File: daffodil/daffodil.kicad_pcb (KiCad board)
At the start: 2 copper layers, 70.7 x 53.3 mm, 8 parts, among them J1 NEIGHBOR1, J2 NEIGHBOR2, J7 BONUS_ROW, P1 GREATFET-PROTO-AREA

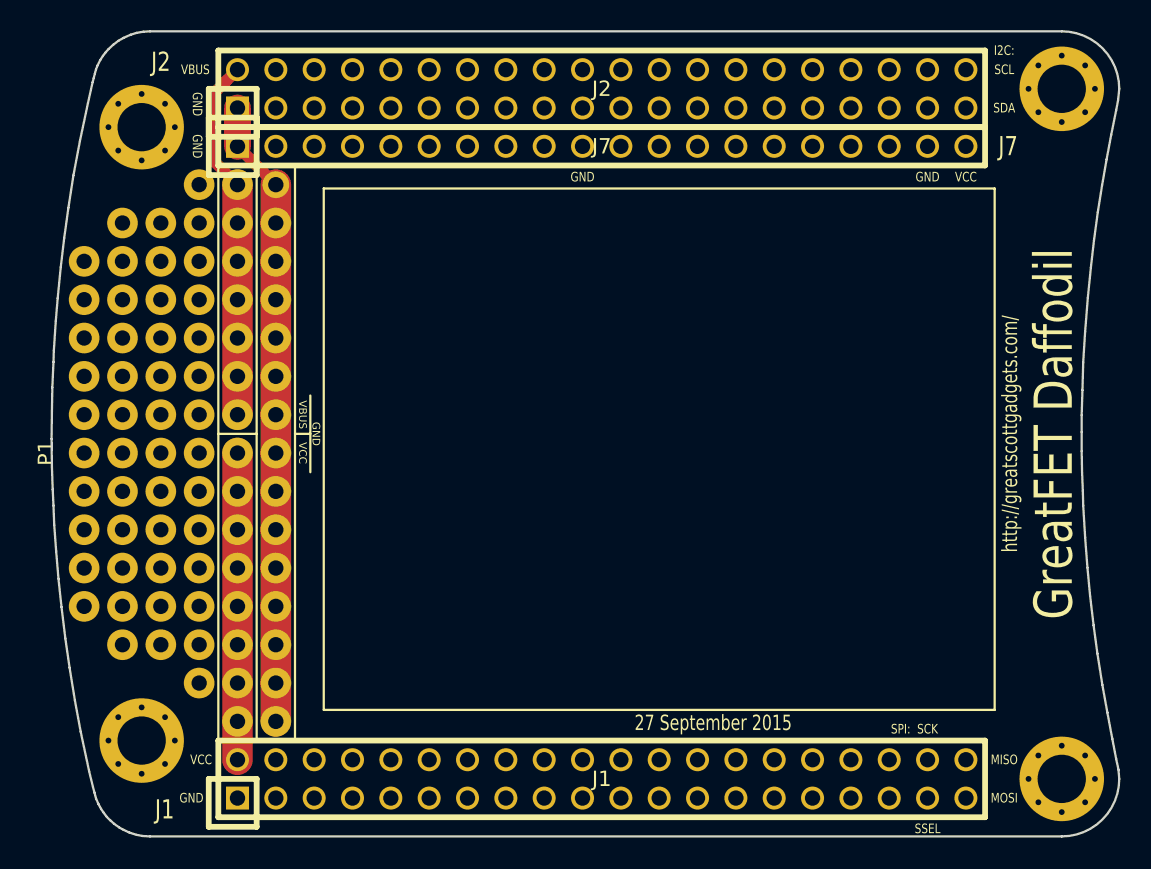
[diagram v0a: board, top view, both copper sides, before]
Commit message: Daffodil: removed GND from J7 pin 10, updated silkscreen
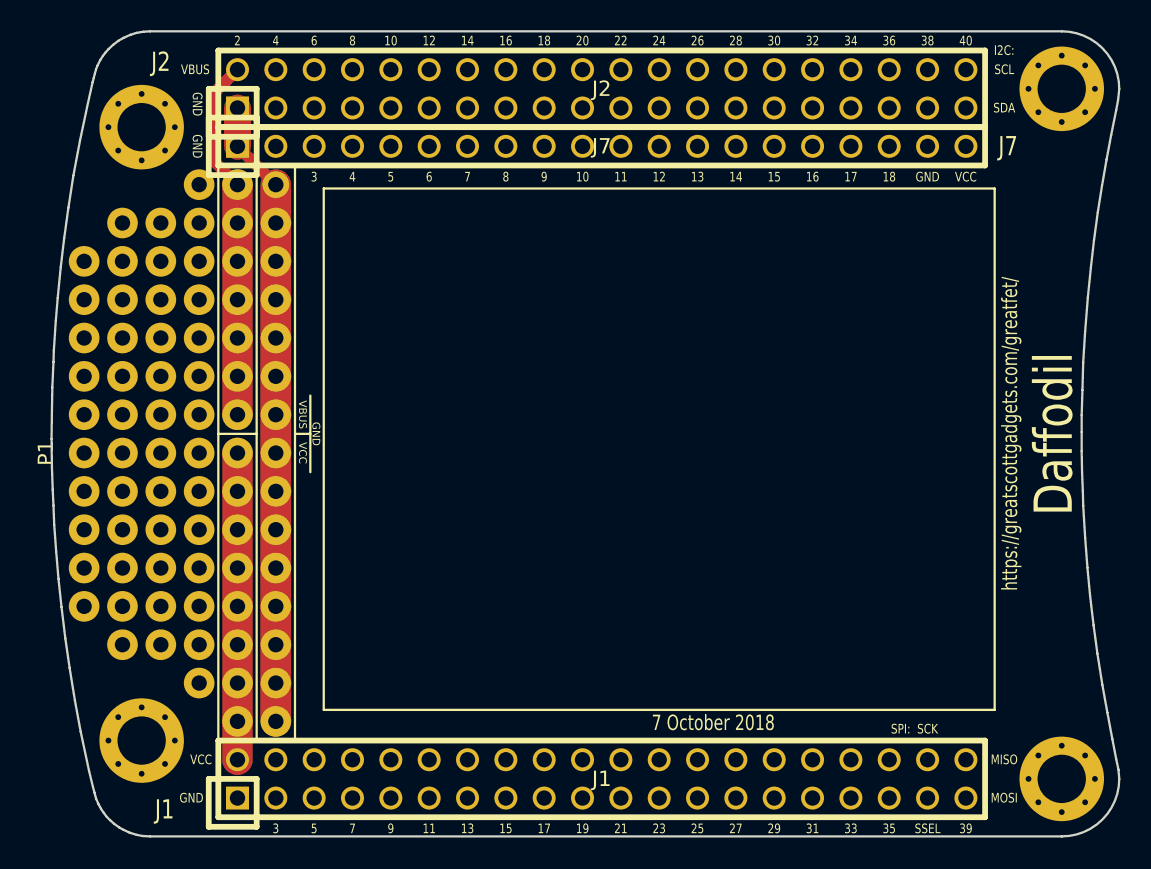
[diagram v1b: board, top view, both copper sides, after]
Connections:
- J7 pad 10: GND -> /32KHZ
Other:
- board text added: "10"
- board text added: "11"
- board text added: "12"
- board text added: "13"
- board text added: "14"
- board text added: "15"
- board text added: "16"
- board text added: "17"
- board text added: "18"
- board text added: "19"
- board text added: "20"
- board text added: "21"
- board text added: "22"
- board text added: "23"
- board text added: "24"
- board text added: "25"
- board text added: "26"
- board text added: "27"
- board text added: "28"
- board text added: "29"
- board text added: "30"
- board text added: "31"
- board text added: "32"
- board text added: "33"
- board text added: "34"
- board text added: "35"
- board text added: "36"
- board text added: "38"
- board text added: "39"
- board text added: "4"
- board text added: "40"
- board text added: "5"
- board text added: "6"
- board text added: "7"
- board text added: "7 October 2018"
- board text added: "8"
- board text added: "9"
- board text added: "Daffodil"
- board text added: "https://greatscottgadgets.com/greatfet/"
- board text removed: "27 September 2015"
- board text removed: "GreatFET Daffodil"
- board text removed: "http://greatscottgadgets.com/"
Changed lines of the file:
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@@
-(kicad_pcb (version 4) (host pcbnew "(2015-08-18 BZR 6102)-product")
+(kicad_pcb (version 4) (host pcbnew 4.0.6)
   (general
-    (links 71)
+    (links 70)
     (no_connects 0)
-    (area 107.95 66.04 279.525801 196.925001)
+    (area 107.95 66.04 279.525801 124.460001)
     (thickness 1.6)
-    (drawings 137)
+    (drawings 190)
     (tracks 34)
     (zones 0)
     (modules 8)
-    (nets 134)
+    (nets 135)
   )
   (page A4)
@@
     (pad_to_paste_clearance_ratio -0.05)
     (aux_axis_origin 0 0)
-    (visible_elements FFFFFF7F)
+    (visible_elements FFFCFF7F)
     (pcbplotparams
       (layerselection 0x010e0_80000001)
@@
   (net 132 "Net-(P1-Pad72)")
   (net 133 "Net-(P1-Pad45)")
+  (net 134 /32KHZ)
   (net_class Default "This is the default net class."
     (clearance 0.3048)
@@
     (uvia_dia 0.508)
     (uvia_drill 0.2032)
+    (add_net /32KHZ)
     (add_net /ADC0_0)
     (add_net /ADC0_2)
@@
       (net 87 /RTC_ALARM))
     (pad 10 thru_hole circle (at -1.27 0) (size 1.524 1.524) (drill 1.016) (layers *.Cu *.Mask F.SilkS)
-      (net 1 GND))
+      (net 134 /32KHZ))
     (pad 11 thru_hole circle (at 1.27 0) (size 1.524 1.524) (drill 1.016) (layers *.Cu *.Mask F.SilkS)
       (net 88 /RESET))
@@
       (net 133 "Net-(P1-Pad45)"))
   )
+  (gr_text 39 (at 170.18 121.412) (layer F.SilkS)
+    (effects (font (size 0.635 0.508) (thickness 0.1016)))
+  )
+  (gr_text 35 (at 165.1 121.412) (layer F.SilkS)
+    (effects (font (size 0.635 0.508) (thickness 0.1016)))
+  )
+  (gr_text 33 (at 162.56 121.412) (layer F.SilkS)
+    (effects (font (size 0.635 0.508) (thickness 0.1016)))
+  )
+  (gr_text 31 (at 160.02 121.412) (layer F.SilkS)
+    (effects (font (size 0.635 0.508) (thickness 0.1016)))
+  )
+  (gr_text 29 (at 157.48 121.412) (layer F.SilkS)
+    (effects (font (size 0.635 0.508) (thickness 0.1016)))
+  )
+  (gr_text 27 (at 154.94 121.412) (layer F.SilkS)
+    (effects (font (size 0.635 0.508) (thickness 0.1016)))
+  )
+  (gr_text 25 (at 152.4 121.412) (layer F.SilkS)
+    (effects (font (size 0.635 0.508) (thickness 0.1016)))
+  )
+  (gr_text 23 (at 149.86 121.412) (layer F.SilkS)
+    (effects (font (size 0.635 0.508) (thickness 0.1016)))
+  )
+  (gr_text 21 (at 147.32 121.412) (layer F.SilkS)
+    (effects (font (size 0.635 0.508) (thickness 0.1016)))
+  )
+  (gr_text 19 (at 144.78 121.412) (layer F.SilkS)
+    (effects (font (size 0.635 0.508) (thickness 0.1016)))
+  )
+  (gr_text 17 (at 142.24 121.412) (layer F.SilkS)
+    (effects (font (size 0.635 0.508) (thickness 0.1016)))
+  )
+  (gr_text 15 (at 139.7 121.412) (layer F.SilkS)
+    (effects (font (size 0.635 0.508) (thickness 0.1016)))
+  )
+  (gr_text 13 (at 137.16 121.412) (layer F.SilkS)
+    (effects (font (size 0.635 0.508) (thickness 0.1016)))
+  )
+  (gr_text 11 (at 134.62 121.412) (layer F.SilkS)
+    (effects (font (size 0.635 0.508) (thickness 0.1016)))
+  )
+  (gr_text 9 (at 132.08 121.412) (layer F.SilkS)
+    (effects (font (size 0.635 0.508) (thickness 0.1016)))
+  )
+  (gr_text 7 (at 129.54 121.412) (layer F.SilkS)
+    (effects (font (size 0.635 0.508) (thickness 0.1016)))
+  )
+  (gr_text 18 (at 165.1 78.232) (layer F.SilkS)
+    (effects (font (size 0.635 0.508) (thickness 0.1016)))
+  )
+  (gr_text 17 (at 162.56 78.232) (layer F.SilkS)
+    (effects (font (size 0.635 0.508) (thickness 0.1016)))
+  )
+  (gr_text 16 (at 160.02 78.232) (layer F.SilkS)
+    (effects (font (size 0.635 0.508) (thickness 0.1016)))
+  )
+  (gr_text 15 (at 157.48 78.232) (layer F.SilkS)
+    (effects (font (size 0.635 0.508) (thickness 0.1016)))
+  )
+  (gr_text 14 (at 154.94 78.232) (layer F.SilkS)
+    (effects (font (size 0.635 0.508) (thickness 0.1016)))
+  )
+  (gr_text 13 (at 152.4 78.232) (layer F.SilkS)
+    (effects (font (size 0.635 0.508) (thickness 0.1016)))
+  )
+  (gr_text 12 (at 149.86 78.232) (layer F.SilkS)
+    (effects (font (size 0.635 0.508) (thickness 0.1016)))
+  )
+  (gr_text 11 (at 147.32 78.232) (layer F.SilkS)
+    (effects (font (size 0.635 0.508) (thickness 0.1016)))
+  )
+  (gr_text 10 (at 144.78 78.232) (layer F.SilkS)
+    (effects (font (size 0.635 0.508) (thickness 0.1016)))
+  )
+  (gr_text 9 (at 142.24 78.232) (layer F.SilkS)
+    (effects (font (size 0.635 0.508) (thickness 0.1016)))
+  )
+  (gr_text 8 (at 139.7 78.232) (layer F.SilkS)
+    (effects (font (size 0.635 0.508) (thickness 0.1016)))
+  )
+  (gr_text 7 (at 137.16 78.232) (layer F.SilkS)
+    (effects (font (size 0.635 0.508) (thickness 0.1016)))
+  )
+  (gr_text 6 (at 134.62 78.232) (layer F.SilkS)
+    (effects (font (size 0.635 0.508) (thickness 0.1016)))
+  )
+  (gr_text 5 (at 132.08 78.232) (layer F.SilkS)
+    (effects (font (size 0.635 0.508) (thickness 0.1016)))
+  )
+  (gr_text 40 (at 170.18 69.215) (layer F.SilkS)
+    (effects (font (size 0.635 0.508) (thickness 0.1016)))
+  )
+  (gr_text 38 (at 167.64 69.215) (layer F.SilkS)
+    (effects (font (size 0.635 0.508) (thickness 0.1016)))
+  )
+  (gr_text 36 (at 165.1 69.215) (layer F.SilkS)
+    (effects (font (size 0.635 0.508) (thickness 0.1016)))
+  )
+  (gr_text 34 (at 162.56 69.215) (layer F.SilkS)
+    (effects (font (size 0.635 0.508) (thickness 0.1016)))
+  )
+  (gr_text 32 (at 160.02 69.215) (layer F.SilkS)
+    (effects (font (size 0.635 0.508) (thickness 0.1016)))
+  )
+  (gr_text 30 (at 157.48 69.215) (layer F.SilkS)
+    (effects (font (size 0.635 0.508) (thickness 0.1016)))
+  )
+  (gr_text 28 (at 154.94 69.215) (layer F.SilkS)
+    (effects (font (size 0.635 0.508) (thickness 0.1016)))
+  )
+  (gr_text 26 (at 152.4 69.215) (layer F.SilkS)
+    (effects (font (size 0.635 0.508) (thickness 0.1016)))
+  )
+  (gr_text 24 (at 149.86 69.215) (layer F.SilkS)
+    (effects (font (size 0.635 0.508) (thickness 0.1016)))
+  )
+  (gr_text 22 (at 147.32 69.215) (layer F.SilkS)
+    (effects (font (size 0.635 0.508) (thickness 0.1016)))
+  )
+  (gr_text 20 (at 144.78 69.215) (layer F.SilkS)
+    (effects (font (size 0.635 0.508) (thickness 0.1016)))
+  )
+  (gr_text 18 (at 142.24 69.215) (layer F.SilkS)
+    (effects (font (size 0.635 0.508) (thickness 0.1016)))
+  )
+  (gr_text 16 (at 139.7 69.215) (layer F.SilkS)
+    (effects (font (size 0.635 0.508) (thickness 0.1016)))
+  )
+  (gr_text 14 (at 137.16 69.215) (layer F.SilkS)
+    (effects (font (size 0.635 0.508) (thickness 0.1016)))
+  )
+  (gr_text 12 (at 134.62 69.215) (layer F.SilkS)
+    (effects (font (size 0.635 0.508) (thickness 0.1016)))
+  )
+  (gr_text 10 (at 132.08 69.215) (layer F.SilkS)
+    (effects (font (size 0.635 0.508) (thickness 0.1016)))
+  )
+  (gr_text 8 (at 129.54 69.215) (layer F.SilkS)
+    (effects (font (size 0.635 0.508) (thickness 0.1016)))
+  )
+  (gr_text 6 (at 127 69.215) (layer F.SilkS)
+    (effects (font (size 0.635 0.508) (thickness 0.1016)))
+  )
+  (gr_text 4 (at 129.54 78.232) (layer F.SilkS)
+    (effects (font (size 0.635 0.508) (thickness 0.1016)))
+  )
+  (gr_text 3 (at 127 78.232) (layer F.SilkS)
+    (effects (font (size 0.635 0.508) (thickness 0.1016)))
+  )
+  (gr_text 4 (at 124.46 69.215) (layer F.SilkS)
+    (effects (font (size 0.635 0.508) (thickness 0.1016)))
+  )
+  (gr_text 2 (at 121.92 69.215) (layer F.SilkS)
+    (effects (font (size 0.635 0.508) (thickness 0.1016)))
+  )
+  (gr_text 5 (at 127 121.412) (layer F.SilkS)
+    (effects (font (size 0.635 0.508) (thickness 0.1016)))
+  )
+  (gr_text 3 (at 124.46 121.412) (layer F.SilkS)
+    (effects (font (size 0.635 0.508) (thickness 0.1016)))
+  )
   (gr_text GND (at 119.253 76.2 270) (layer F.SilkS)
     (effects (font (size 0.635 0.508) (thickness 0.1016)))
@@
   )
   (gr_text GND (at 167.64 78.232) (layer F.SilkS)
-    (effects (font (size 0.635 0.508) (thickness 0.1016)))
-  )
-  (gr_text GND (at 144.78 78.232) (layer F.SilkS)
     (effects (font (size 0.635 0.508) (thickness 0.1016)))
   )
@@
   (gr_line (start 177.9016 92.3544) (end 177.8508 94.0054) (angle 90) (layer Edge.Cuts) (width 0.15))
   (gr_line (start 177.9524 90.5002) (end 177.9016 92.3544) (angle 90) (layer Edge.Cuts) (width 0.15))
-  (gr_text "27 September 2015" (at 153.4414 114.4016) (layer F.SilkS)
+  (gr_text "7 October 2018" (at 153.4414 114.4016) (layer F.SilkS)
     (effects (font (size 1.016 0.762) (thickness 0.1524)))
   )
@@
     (effects (font (size 1.016 1.016) (thickness 0.1778)))
   )
-  (gr_text http://greatscottgadgets.com/ (at 173.101 95.25 90) (layer F.SilkS)
+  (gr_text https://greatscottgadgets.com/greatfet/ (at 173.101 95.25 90) (layer F.SilkS)
     (effects (font (size 1.016 0.762) (thickness 0.1524)))
   )
@@
   (gr_arc (start 176.53 118.11) (end 180.34 118.11) (angle 90) (layer Edge.Cuts) (width 0.15))
   (gr_arc (start 279.4508 95.25) (end 177.8508 95.25) (angle 12.5) (layer Cmts.User) (width 0.15))
-  (gr_text "GreatFET Daffodil" (at 176.022 95.25 90) (layer F.SilkS)
+  (gr_text Daffodil (at 176.022 95.25 90) (layer F.SilkS)
     (effects (font (size 2.54 2.032) (thickness 0.381)))
   )

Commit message: Updated Daffodil silkscreen, porto area, and breadboard.
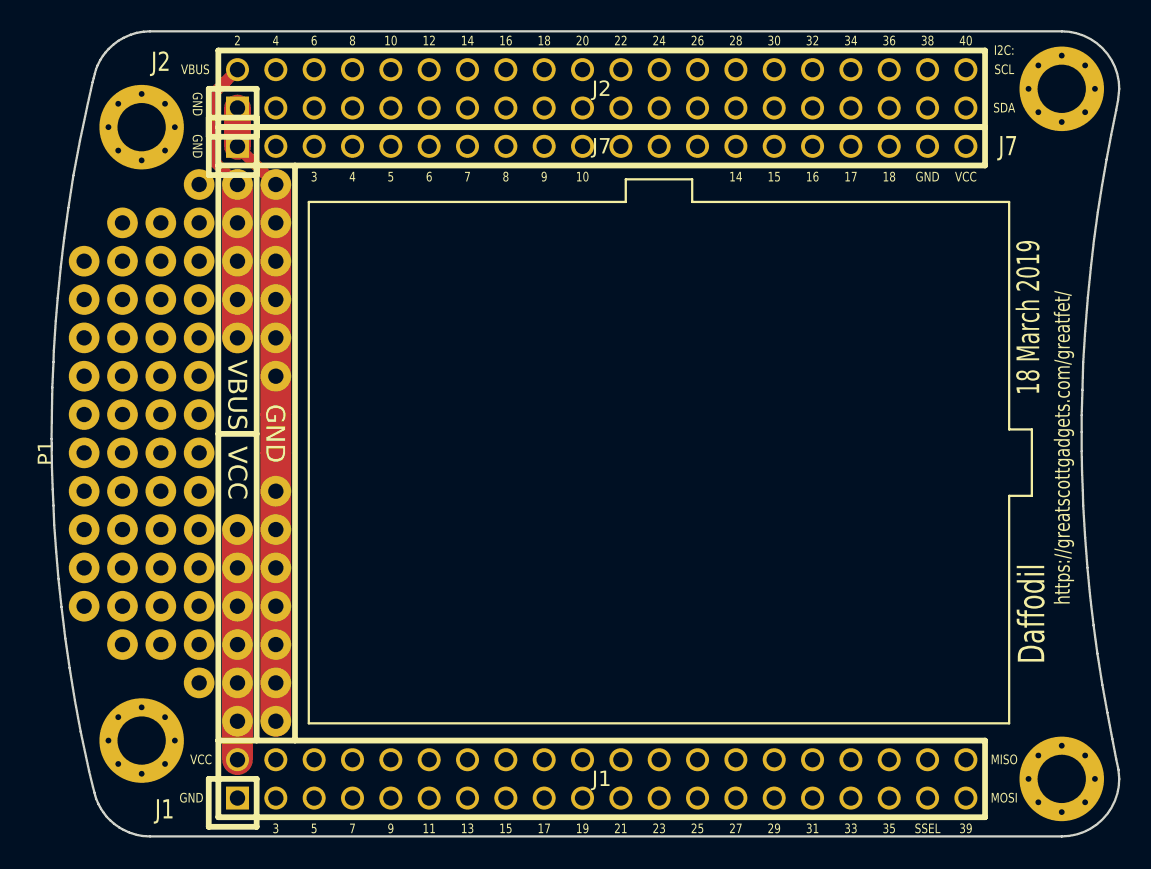
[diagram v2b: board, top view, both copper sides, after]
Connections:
- P1 pad 14: GND -> /VBUS
- P1 pad 15: GND -> /VBUS
- P1 pad 19: /VBUS -> VCC
- P1 pad 20: /VBUS -> VCC
- P1 pad 21: /VBUS -> VCC
- P1 pad 22: /VBUS -> VCC
- P1 pad 25: VCC -> Net-(P1-Pad25)
- P1 pad 26: VCC -> Net-(P1-Pad26)
- P1 pad 27: VCC -> Net-(P1-Pad27)
- P1 pad 28: VCC -> Net-(P1-Pad28)
- P1 pad 29: VCC -> Net-(P1-Pad29)
- P1 pad 30: VCC -> Net-(P1-Pad30)
- P1 pad 63: (no net) -> Net-(P1-Pad63)
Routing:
- net VCC: track 20.3 -> 15.2 mm
- net /VBUS: track 24.3 -> 19.2 mm
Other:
- board text added: "18 March 2019"
- board text removed: "7 October 2018"
- board text removed: "SCK"
- board text removed: "SPI:"
